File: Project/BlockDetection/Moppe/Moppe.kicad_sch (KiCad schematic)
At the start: 53 parts, among them J1 Conn_01x02_Pin, J2 Conn_01x02_Pin, J3 Conn_01x02_Pin, J4 Conn_01x02_Pin, J5 Conn_01x02_Pin, J6 Conn_01x02_Pin, J7 Conn_01x04_Socket, J8 RJ45, J9 RJ45, Q1 BC557, Q2 BC557, Q3 BC557, Q4 BC557, U1 PC847, U3 ESP32-C3-WROOM-02, U4 LT1129-3.3_SOT223, U5 4N35, U6 MAX3485

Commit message: DIY Hideout
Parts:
- added U2: LTV-847S, Package_DIP:SMDIP-16_W9.53mm, symbol Isolator:LTV-847S
- C3: value 3,3µF -> 10µF
- U4: value LT1129-3.3_SOT223 -> Mini560 Pro
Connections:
- net GND: now also C4.2, J3.1 (Pin_1), U1.2
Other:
- moved on the sheet: C1, C2, J7, JP1, R10, R11, R12, R14, R15, R9, U5, U6

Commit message: check
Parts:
- added TP1, TP2, TP3, TP4, TP5, TP6, TP7, TP8: TestPoint_Alt, symbol Connector:TestPoint_Alt
- added unit 4 of U3
- added unit 2 of U3
- added unit 3 of U3
- renumbered C4 to C1, C5 to C2, C6 to C3, C7 to C4, C2 to C5, C1 to C6, C3 to C7, D2 to D1, D1 to D2, D6 to D5, D5 to D6, J4 to J1, J1 to J3, J3 to J4, R13 to R1, R15 to R10, R12 to R11, R14 to R12, R10 to R13, R9 to R14, R11 to R15, R1 to R3, R3 to R4, R4 to R5, R5 to R6, R6 to R7, R7 to R8, R8 to R9, U5 to U2, U2 to U3, U3 to U4, U6 to U5, U4 to U6
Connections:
- net +3V3: now also U4.2 (EN)
- net DCC Track_0 Power: now also D2.1 (K), D6.2 (A), J4.2 (Pin_2), R3.2
- net DCC Track_1 Power: now also D1.1 (K), D5.2 (A), J1.2 (Pin_2), R2.2
- net DCC Track_2 Power: now also D3.1 (K), D7.2 (A), J5.2 (Pin_2), R4.2
- net at U1.16, U4.18 (IO0): now also TP5.1
- net DCC Power: now reaches D1.2 (A), D3.2 (A), D4.2 (A), D5.1 (K), D7.1 (K), D8.1 (K), J2.2 (Pin_2), Q2.3 (E), Q3.3 (E), Q4.3 (E)
- net DCC Power: now also D2.2 (A), D6.1 (K), J3.2 (Pin_2), Q1.3 (E)
- net at C3.1, Q3.1 (C), R8.2: now also TP3.1
- net at C1.1, Q1.1 (C), R6.2: now also TP1.1
- net at C2.1, Q2.1 (C), R7.2: now also TP2.1
- net at U1.12, U4.16 (IO2): now also TP7.1
- net at U1.14, U4.17 (IO1): now also TP6.1
- net at U1.10, U4.15 (IO3): now also TP8.1
- net at C4.1, Q4.1 (C), R9.2: now also TP4.1
- net GND renamed DCC Gnd
- no-connect marks 10 -> 31
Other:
- moved on the sheet: U2, U3A

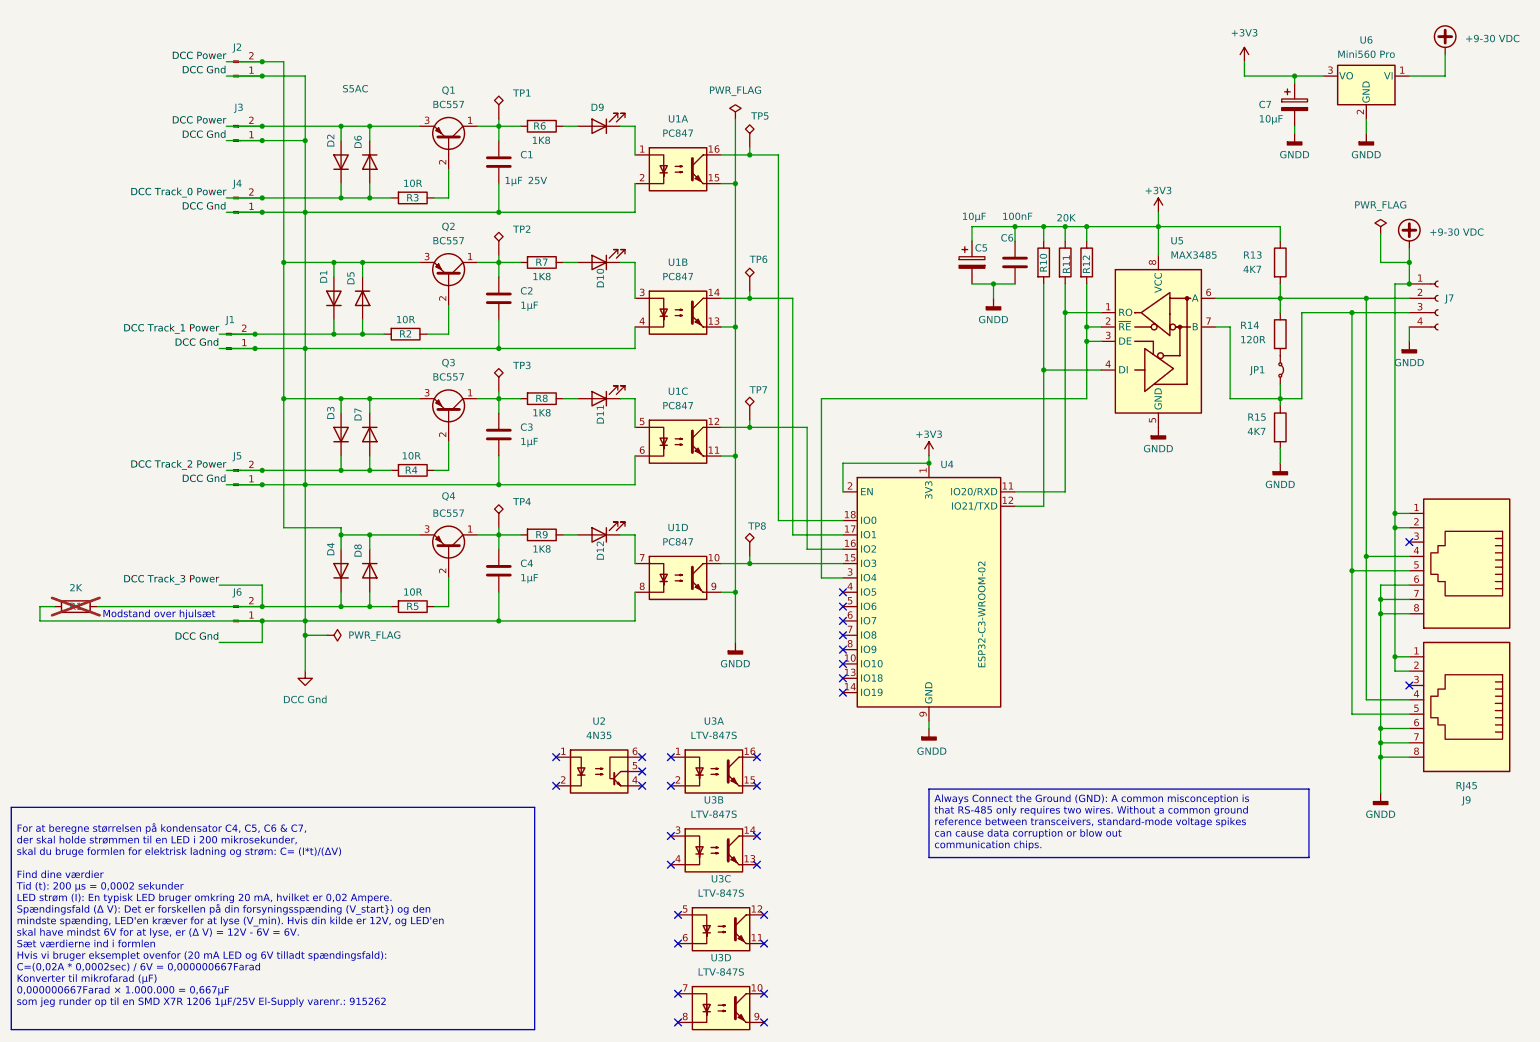
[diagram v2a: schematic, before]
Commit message: Programming MCU i kredssløb
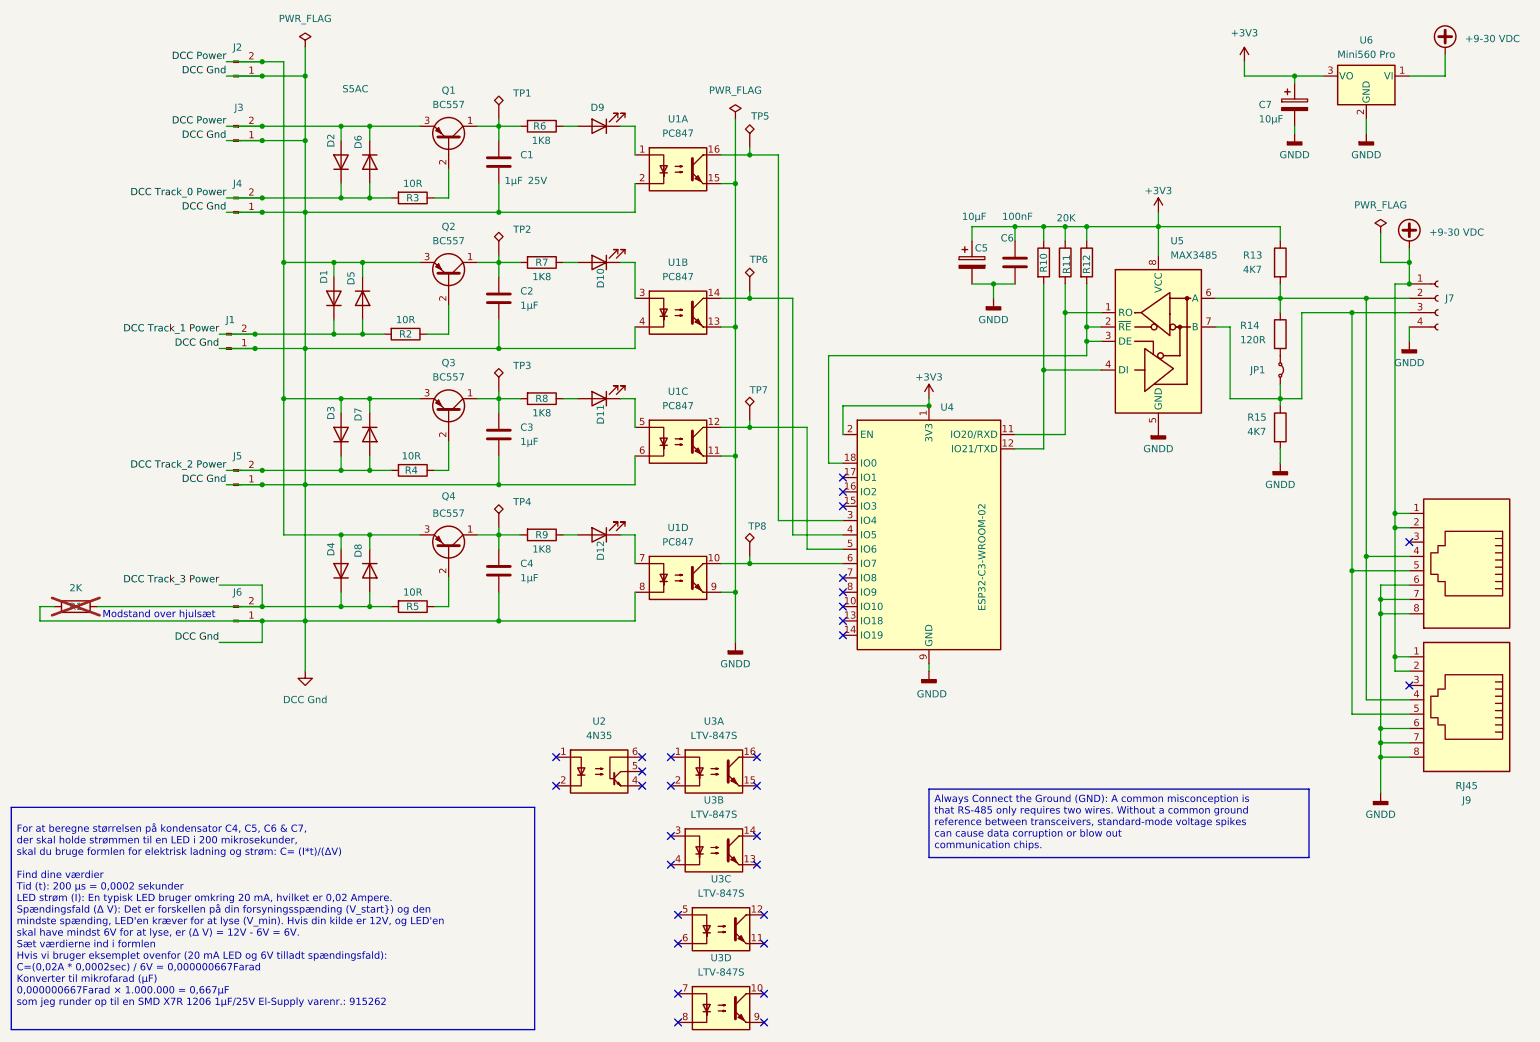
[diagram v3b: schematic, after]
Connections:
- net at TP5.1, U1.16: now also U4.3 (IO4); no longer U4.18 (IO0)
- net at TP7.1, U1.12: now also U4.5 (IO6); no longer U4.16 (IO2)
- net at TP6.1, U1.14: now also U4.4 (IO5); no longer U4.17 (IO1)
- net at TP8.1, U1.10: now also U4.6 (IO7); no longer U4.15 (IO3)
- net at R12.2, U5.2 (~{RE}), U5.3 (DE): now also U4.18 (IO0); no longer U4.3 (IO4)
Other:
- moved on the sheet: U4

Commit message: Programming MCU i kredssløb
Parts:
- added R16: 10k, Inductor_THT:L_CommonMode_PulseElectronics_PH9455x105NL_1, symbol Device:R
- added R17, R18: 1K, Inductor_THT:L_CommonMode_PulseElectronics_PH9455x105NL_1, symbol Device:R
- added TP10, TP11, TP9: TestPoint_Alt, symbol Connector:TestPoint_Alt
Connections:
- net +3V3: now also R16.1; no longer U4.2 (EN)
- net at R10.2, U5.4 (DI): now also R17.1; no longer U4.12 (IO21/TXD)
- net at R11.2, U5.1 (RO): now also R18.1; no longer U4.11 (IO20/RXD)
- net at U4.8 (IO9): now also TP9.1
- new net: R17.2, TP11.1, U4.12 (IO21/TXD)
- new net: R16.2, U4.2 (EN)
- new net: R18.2, TP10.1, U4.11 (IO20/RXD)
- no-connect marks 31 -> 30

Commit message: moppe
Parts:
- removed TP10, TP11, TP9: TestPoint_Alt, symbol Connector:TestPoint_Alt
- added TP10: Reset, Relay_THT:Relay_DPDT_Schrack-RT2-FormC_RM5mm, symbol Connector:TestPoint_Probe
- added TP11: Program Tx, Relay_THT:Relay_DPDT_Schrack-RT2-FormC_RM5mm, symbol Connector:TestPoint_Probe
- added TP12: Program Rx, Relay_THT:Relay_DPDT_Schrack-RT2-FormC_RM5mm, symbol Connector:TestPoint_Probe
- added TP13, TP14: TestPoint_Alt, symbol Connector:TestPoint_Alt
- added TP9: Program, symbol Connector:TestPoint_Probe
- renumbered R16 to R10, R10 to R11, R17 to R12, R11 to R13, R18 to R14, R12 to R15, R13 to R16, R14 to R17, R15 to R18, U2 to U1, U1 to U2
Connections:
- net +3V3: now also TP14.1
- net GNDD: now also TP13.1
- net at R12.2, U4.12 (IO21/TXD): now also TP12.1
- net at R10.2, U4.2 (EN): now also TP10.1
- net at U4.8 (IO9): now also TP9.1
- net at R14.2, U4.11 (IO20/RXD): now also TP11.1

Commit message: SporBesat a la´ Moppe
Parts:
- added TP11: Pg 3.3V, Relay_THT:Relay_DPDT_Schrack-RT2-FormC_RM5mm, symbol Connector:TestPoint_Probe
- added TP12: Pg Gnd, Relay_THT:Relay_DPDT_Schrack-RT2-FormC_RM5mm, symbol Connector:TestPoint_Probe
- TP10: value Reset -> Pg Reset
- TP13: renamed from TP11; value Program Tx -> Pg Tx
- TP14: renamed from TP12; value Program Rx -> Pg Rx
- TP9: value Program -> Pg Mode
- renumbered TP13 to TP15, TP14 to TP16
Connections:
- net +3V3: now also TP11.1
- net GNDD: now also TP12.1
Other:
- moved on the sheet: C5, C6, R11, R12, R13, R14, R15, TP13, TP14, U5
